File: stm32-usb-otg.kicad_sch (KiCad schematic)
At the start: 18 parts

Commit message: Connected LED as a status indicator to the schematic.
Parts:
- added D?: Blue, symbol Device:LED_Small
- added R?: 1k5, symbol Device:R_Small_US
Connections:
- net GND: now also R?.2
- net LED_STATUS: now also D?.2 (A)
- new net: D?.1 (K), R?.1
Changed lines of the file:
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@@
+    (stroke (width 0) (type default) (color 0 0 0 0))
+  )
+  (wire (pts (xy 200.66 142.24) (xy 200.66 143.51))
     (stroke (width 0) (type default) (color 0 0 0 0))
   )
@@
     (stroke (width 0) (type default) (color 0 0 0 0))
   )
+  (wire (pts (xy 200.66 153.67) (xy 200.66 154.94))
+    (stroke (width 0) (type default) (color 0 0 0 0))
+  )
   (wire (pts (xy 118.11 85.09) (xy 118.11 88.9))
     (stroke (width 0) (type default) (color 0 0 0 0))
@@
   )
   (wire (pts (xy 157.48 121.92) (xy 140.97 121.92))
+    (stroke (width 0) (type default) (color 0 0 0 0))
+  )
+  (wire (pts (xy 193.04 142.24) (xy 200.66 142.24))
     (stroke (width 0) (type default) (color 0 0 0 0))
   )
@@
     )
   )
+  (global_label "LED_STATUS" (shape input) (at 193.04 142.24 180) (fields_autoplaced)
+    (effects (font (size 1.27 1.27)) (justify right))
+    (property "Intersheet References" "${INTERSHEET_REFS}" (id 0) (at 179.4388 142.3194 0)
+      (effects (font (size 1.27 1.27)) (justify right) hide)
+    )
+  )
   (global_label "USB_D_-" (shape input) (at 157.48 121.92 0) (fields_autoplaced)
     (effects (font (size 1.27 1.27)) (justify left))
@@
     )
     (pin "1")
+  )
+  (symbol (lib_id "Device:R_Small_US") (at 200.66 151.13 0) (unit 1)
+    (in_bom yes) (on_board yes) (fields_autoplaced)
+    (property "Reference" "R?" (id 0) (at 203.2 149.8599 0)
+      (effects (font (size 1.27 1.27)) (justify left))
+    )
+    (property "Value" "1k5" (id 1) (at 203.2 152.3999 0)
+      (effects (font (size 1.27 1.27)) (justify left))
+    )
+    (property "Footprint" "" (id 2) (at 200.66 151.13 0)
+      (effects (font (size 1.27 1.27)) hide)
+    )
+    (property "Datasheet" "~" (id 3) (at 200.66 151.13 0)
+      (effects (font (size 1.27 1.27)) hide)
+    )
+    (pin "1")
+    (pin "2")
   )
   (symbol (lib_id "Device:C_Small") (at 38.1 78.74 0) (unit 1)
@@
     (pin "2")
   )
+  (symbol (lib_id "power:GND") (at 200.66 154.94 0) (unit 1)
+    (in_bom yes) (on_board yes) (fields_autoplaced)
+    (property "Reference" "#PWR?" (id 0) (at 200.66 161.29 0)
+      (effects (font (size 1.27 1.27)) hide)
+    )
+    (property "Value" "GND" (id 1) (at 200.66 160.02 0))
+    (property "Footprint" "" (id 2) (at 200.66 154.94 0)
+      (effects (font (size 1.27 1.27)) hide)
+    )
+    (property "Datasheet" "" (id 3) (at 200.66 154.94 0)
+      (effects (font (size 1.27 1.27)) hide)
+    )
+    (pin "1")
+  )
   (symbol (lib_id "power:GND") (at 99.06 115.57 0) (unit 1)
     (in_bom yes) (on_board yes) (fields_autoplaced)
@@
     (pin "1")
   )
+  (symbol (lib_id "Device:LED_Small") (at 200.66 146.05 90) (unit 1)
+    (in_bom yes) (on_board yes) (fields_autoplaced)
+    (property "Reference" "D?" (id 0) (at 203.2 144.7164 90)
+      (effects (font (size 1.27 1.27)) (justify right))
+    )
+    (property "Value" "Blue" (id 1) (at 203.2 147.2564 90)
+      (effects (font (size 1.27 1.27)) (justify right))
+    )
+    (property "Footprint" "" (id 2) (at 200.66 146.05 90)
+      (effects (font (size 1.27 1.27)) hide)
+    )
+    (property "Datasheet" "~" (id 3) (at 200.66 146.05 90)
+      (effects (font (size 1.27 1.27)) hide)
+    )
+    (pin "1")
+    (pin "2")
+  )
   (symbol (lib_id "Device:C_Small") (at 55.88 165.1 0) (unit 1)
     (in_bom yes) (on_board yes) (fields_autoplaced)
@@
       (reference "#PWR?") (unit 1) (value "+3V3") (footprint "")
     )
+    (path "/a6164d79-af78-4616-88f6-fd1b2984b009"
+      (reference "#PWR?") (unit 1) (value "GND") (footprint "")
+    )
     (path "/a817d156-816f-4930-9c07-b8f1a48dc112"
       (reference "#PWR?") (unit 1) (value "GND") (footprint "")
@@
       (reference "C?") (unit 1) (value "1n") (footprint "")
     )
+    (path "/fb7a33f8-15cf-4195-94a7-e1e6bcda4c0c"
+      (reference "D?") (unit 1) (value "Blue") (footprint "")
+    )
     (path "/4603151c-6765-4bee-b52a-c7f6f5ee0fc1"
       (reference "L?") (unit 1) (value "39n") (footprint "")
     )
+    (path "/2d40ab7e-9615-42ed-83c9-8ff3d3b318c9"
+      (reference "R?") (unit 1) (value "1k5") (footprint "")
+    )
     (path "/ab52a597-98fb-4e70-adc1-b3659bc73e74"

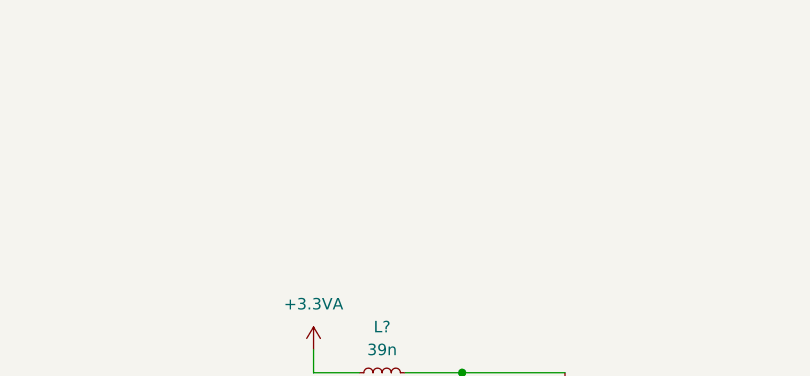
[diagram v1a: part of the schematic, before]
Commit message: Added a custom schematic symbol for the buck regulator.
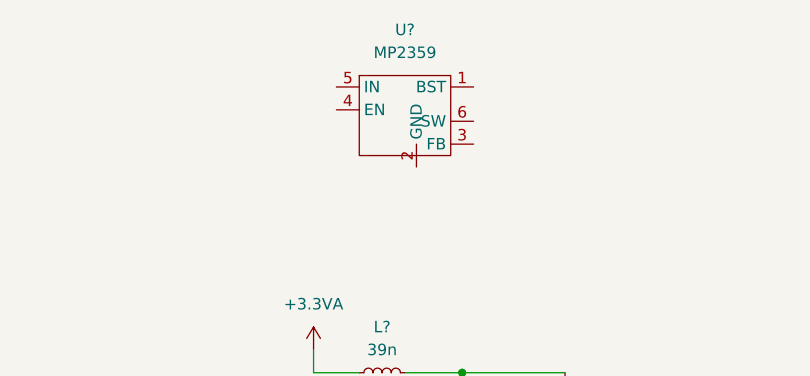
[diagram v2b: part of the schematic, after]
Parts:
- added U?: MP2359, symbol SK:MP2359
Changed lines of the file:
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@@
     (pin "2")
+  )
+  (symbol (lib_id "SK:MP2359") (at 86.36 40.64 0) (unit 1)
+    (in_bom yes) (on_board yes) (fields_autoplaced)
+    (property "Reference" "U?" (id 0) (at 85.09 33.02 0))
+    (property "Value" "MP2359" (id 1) (at 85.09 35.56 0))
+    (property "Footprint" "" (id 2) (at 86.36 36.83 0)
+      (effects (font (size 1.27 1.27)) hide)
+    )
+    (property "Datasheet" "" (id 3) (at 86.36 36.83 0)
+      (effects (font (size 1.27 1.27)) hide)
+    )
+    (pin "1")
+    (pin "2")
+    (pin "3")
+    (pin "4")
+    (pin "5")
+    (pin "6")
   )
   (symbol (lib_id "power:GND") (at 200.66 154.94 0) (unit 1)
@@
       (reference "U?") (unit 1) (value "STM32F405RGT6") (footprint "Package_QFP:LQFP-64_10x10mm_P0.5mm")
     )
+    (path "/9c8a9efe-6b90-497f-baa0-5232f133ccf9"
+      (reference "U?") (unit 1) (value "MP2359") (footprint "")
+    )
     (path "/e33eed0e-7070-405a-a0d6-f3624dae8765"

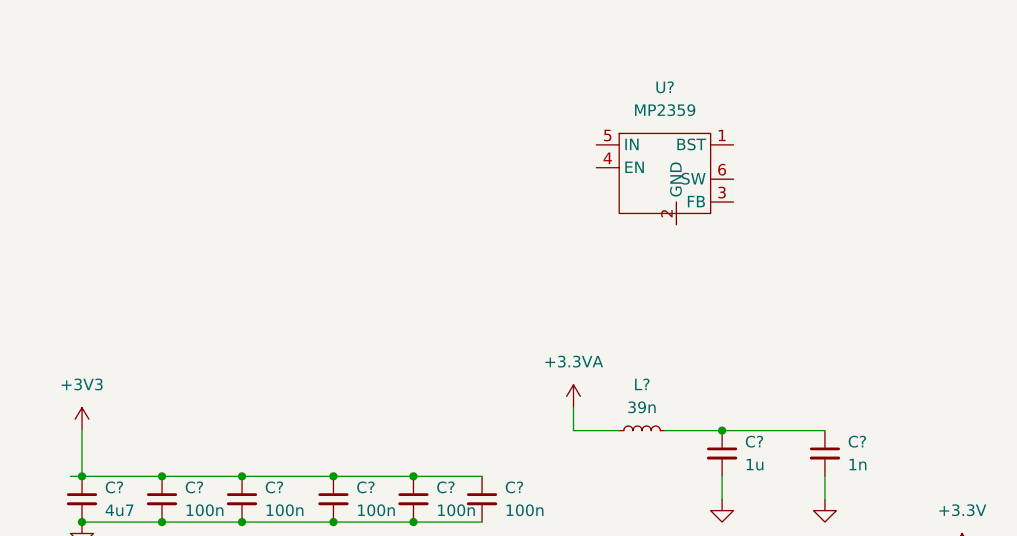
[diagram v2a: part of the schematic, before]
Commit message: Added parts of the buck convertor.
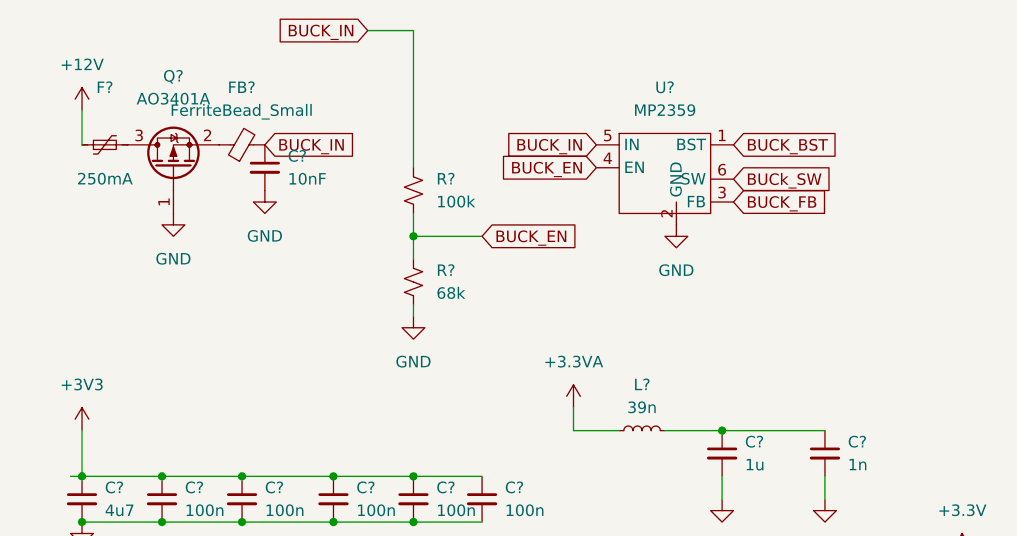
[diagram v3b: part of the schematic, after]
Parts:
- added C?: 10nF, symbol Device:C_Small
- added F?: 250mA, symbol Device:Polyfuse_Small
- added FB?: FerriteBead_Small, symbol Device:FerriteBead_Small
- added Q?: AO3401A, Package_TO_SOT_SMD:SOT-23, symbol Transistor_FET:AO3401A
- added R?: 100k, symbol Device:R_Small_US
- added R?: 68k, symbol Device:R_Small_US
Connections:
- net GND: now also U?.2 (GND), C?.2, Q?.1 (G), R?.2
- net BUCK_BST: now reaches U?.1 (BST)
- net BUCK_FB: now reaches U?.3 (FB)
- net BUCK_EN: now reaches U?.4 (EN)
- net BUCK_EN: now also R?.1, R?.2
- net BUCK_IN: now reaches U?.5 (IN)
- net BUCK_IN: now also C?.1, FB?.2, R?.1
- net BUCk_SW: now reaches U?.6 (SW)
- new net: FB?.1, Q?.2 (S)
- new net: F?.2, Q?.3 (D)
- new net +12V: F?.1

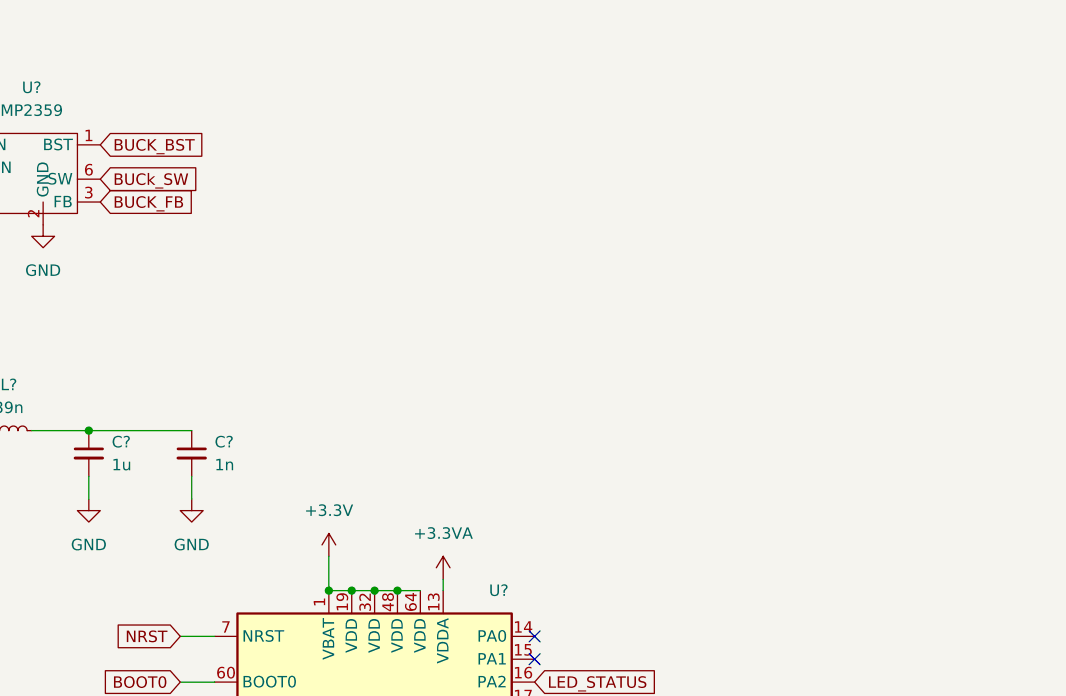
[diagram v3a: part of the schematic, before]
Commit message: Completd the ckt for the Buck regulator.
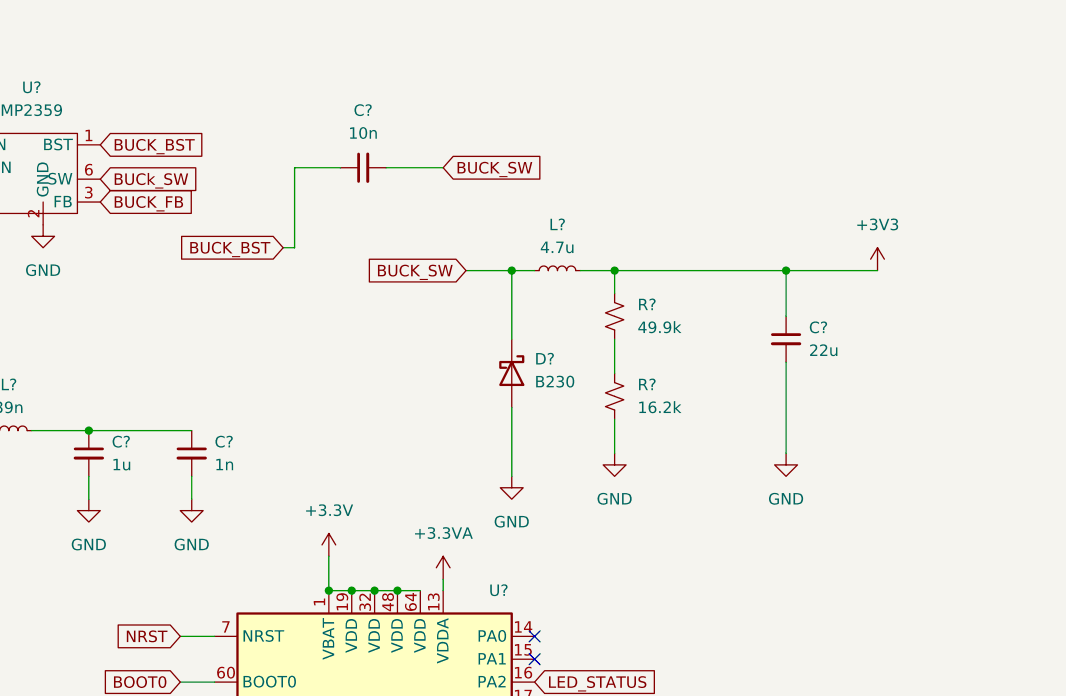
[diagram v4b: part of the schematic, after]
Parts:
- added C?: 10n, symbol Device:C_Small
- added C?: 22u, symbol Device:C_Small
- added D?: B230, Diode_SMD:D_SMB, symbol Diode:B230
- added L?: 4.7u, symbol Device:L_Small
- added R?: 16.2k, symbol Device:R_Small_US
- added R?: 49.9k, symbol Device:R_Small_US
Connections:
- net +3V3: now also C?.1, L?.2, R?.1
- net BUCK_BST: now also C?.1
- net GND: now also C?.2, D?.2 (A), R?.2
- new net: R?.1, R?.2
- new net BUCK_SW: C?.2, D?.1 (K), L?.1

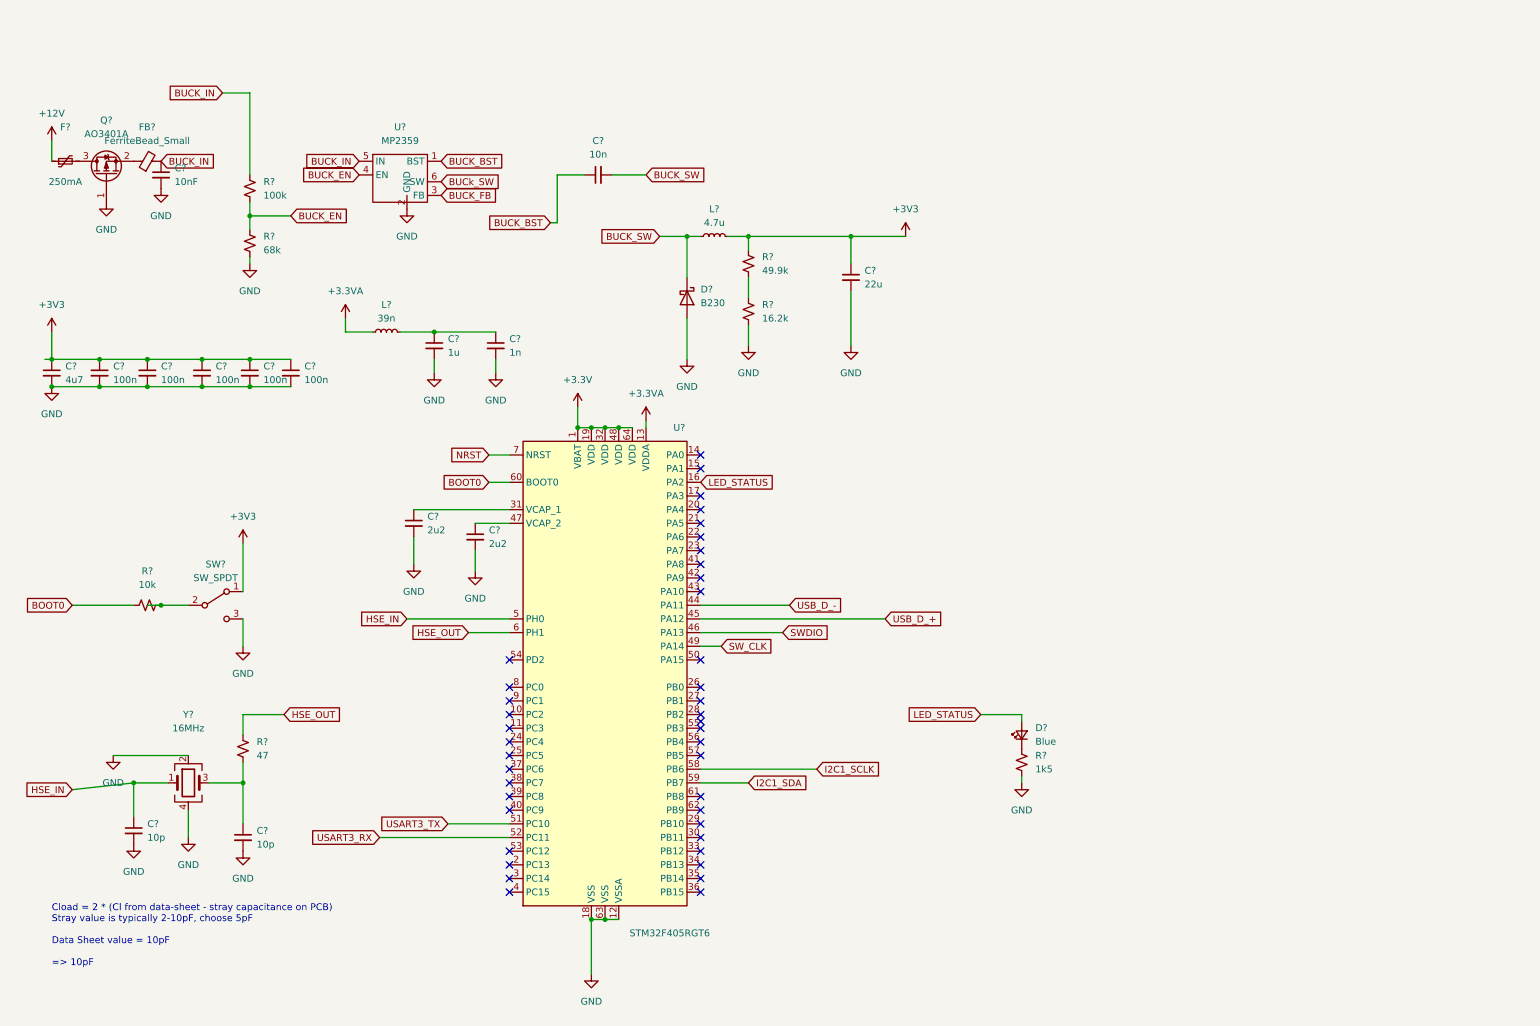
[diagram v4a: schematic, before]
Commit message: Added power connector.
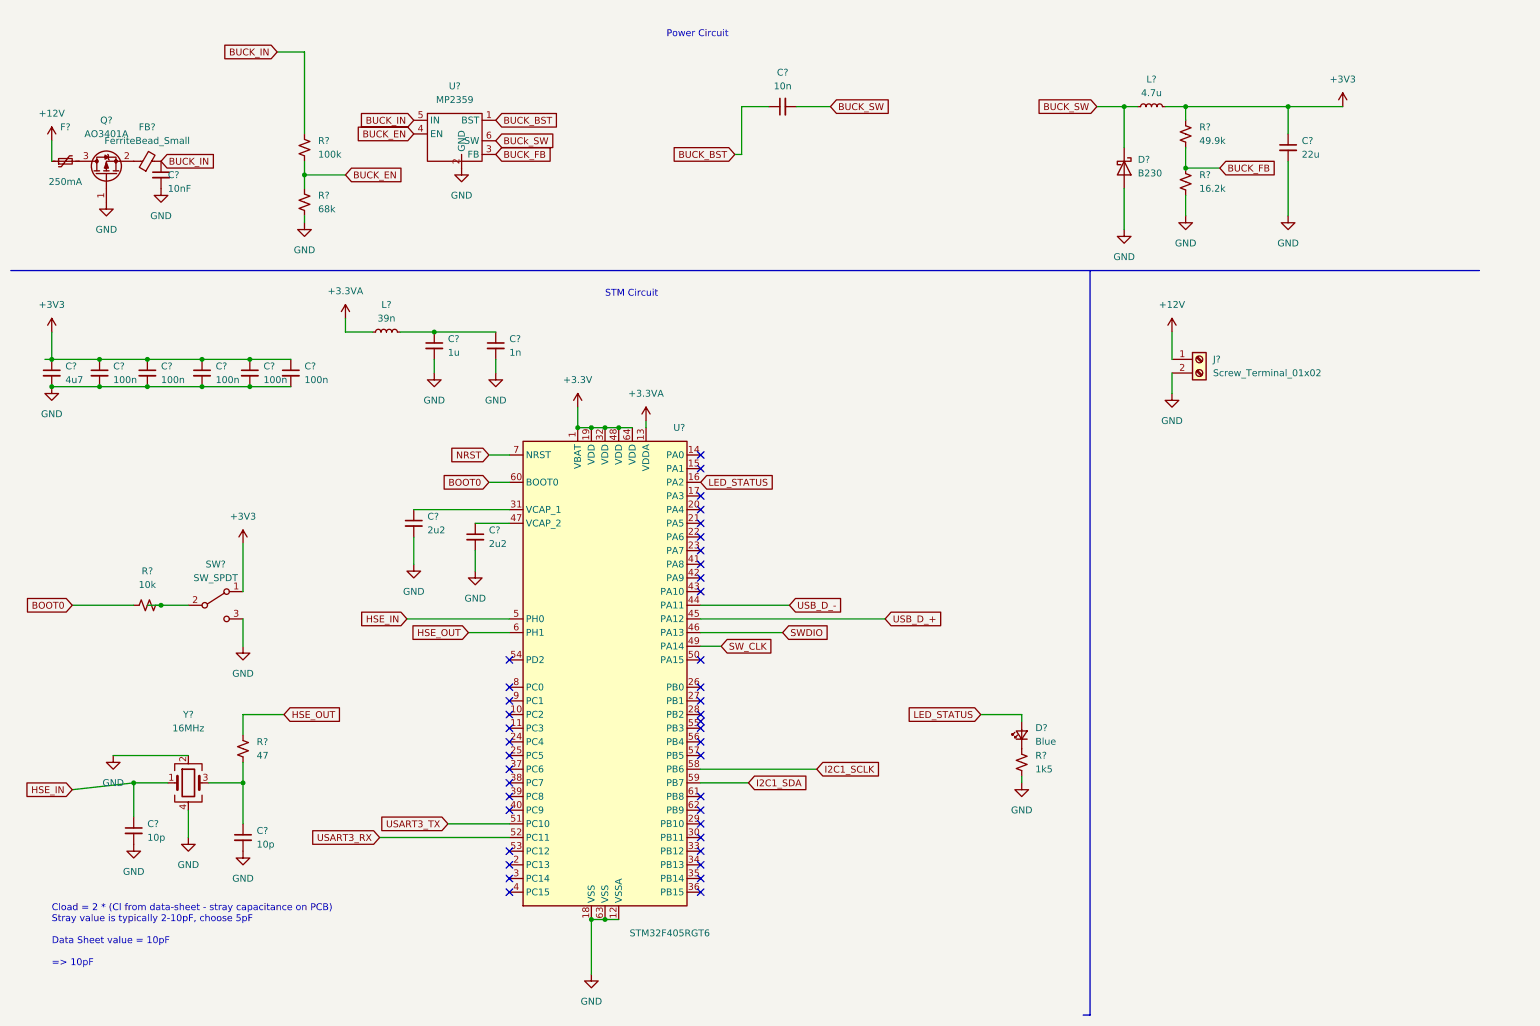
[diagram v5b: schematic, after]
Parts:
- added J?: Screw_Terminal_01x02, symbol Connector:Screw_Terminal_01x02
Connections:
- net +12V: now also J?.1 (Pin_1)
- net BUCK_FB: now also R?.1, R?.2
- net GND: now also J?.2 (Pin_2)
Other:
- note added: "Power Circuit"
- note added: "STM Circuit"
- moved on the sheet: C?, D?, L?, R?, U?
